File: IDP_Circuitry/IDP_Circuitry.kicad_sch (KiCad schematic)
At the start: 4 parts, among them U2 CD4093BE

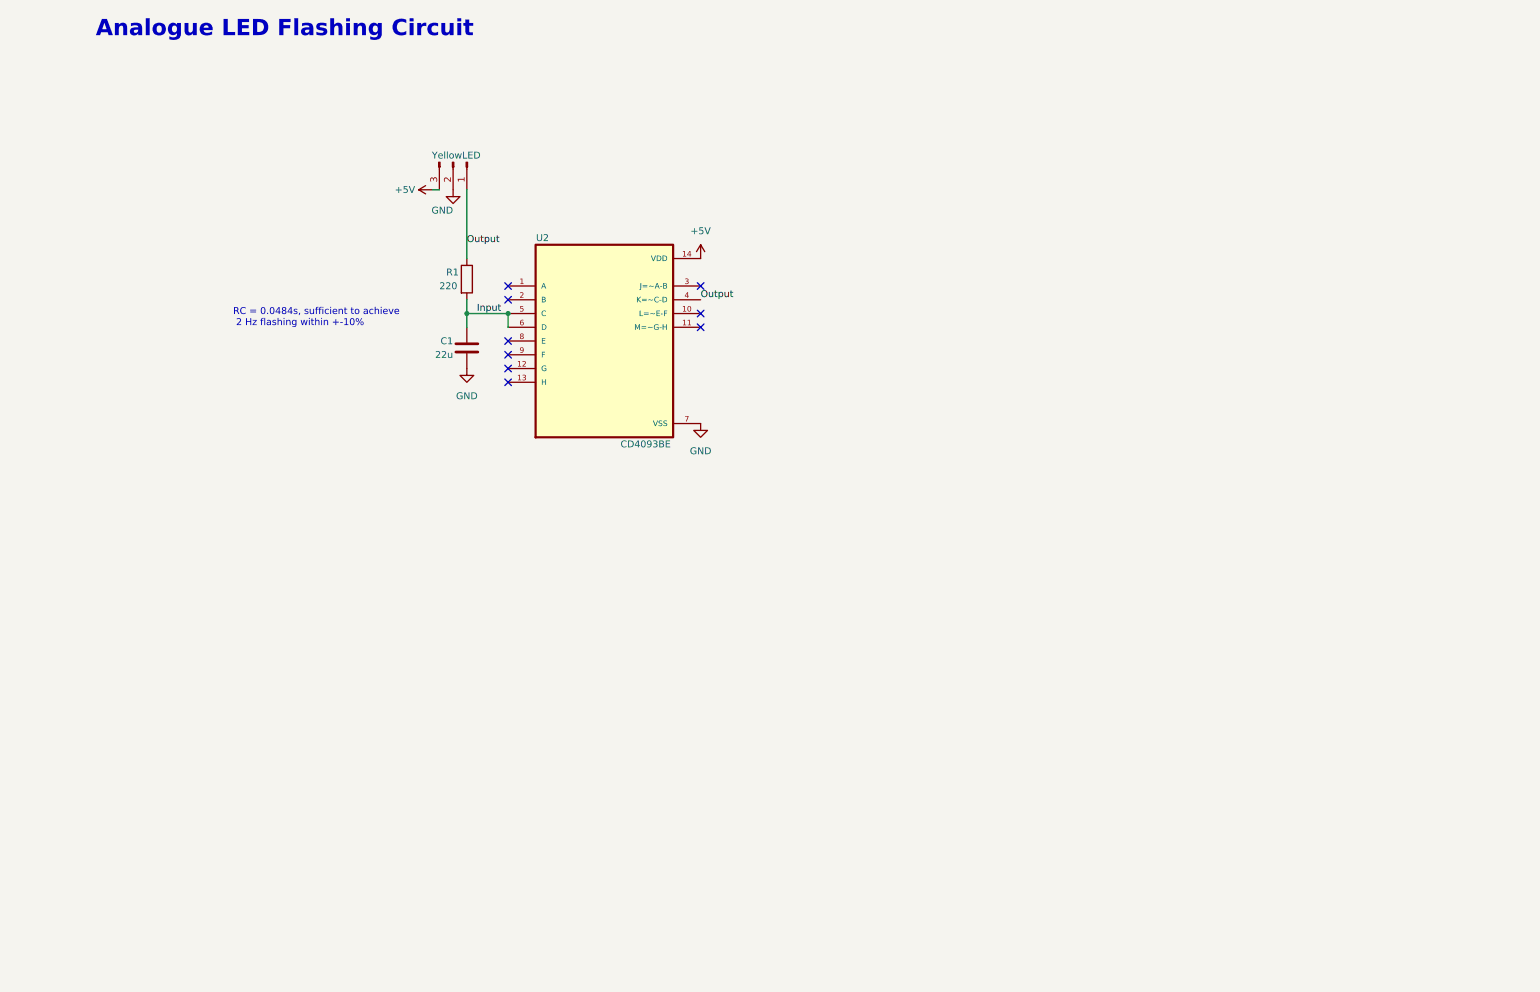
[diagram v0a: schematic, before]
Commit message: Corrected resistor values, changed schmitt NAND gate used, and adjusted schematic to fit all components on the same sheet
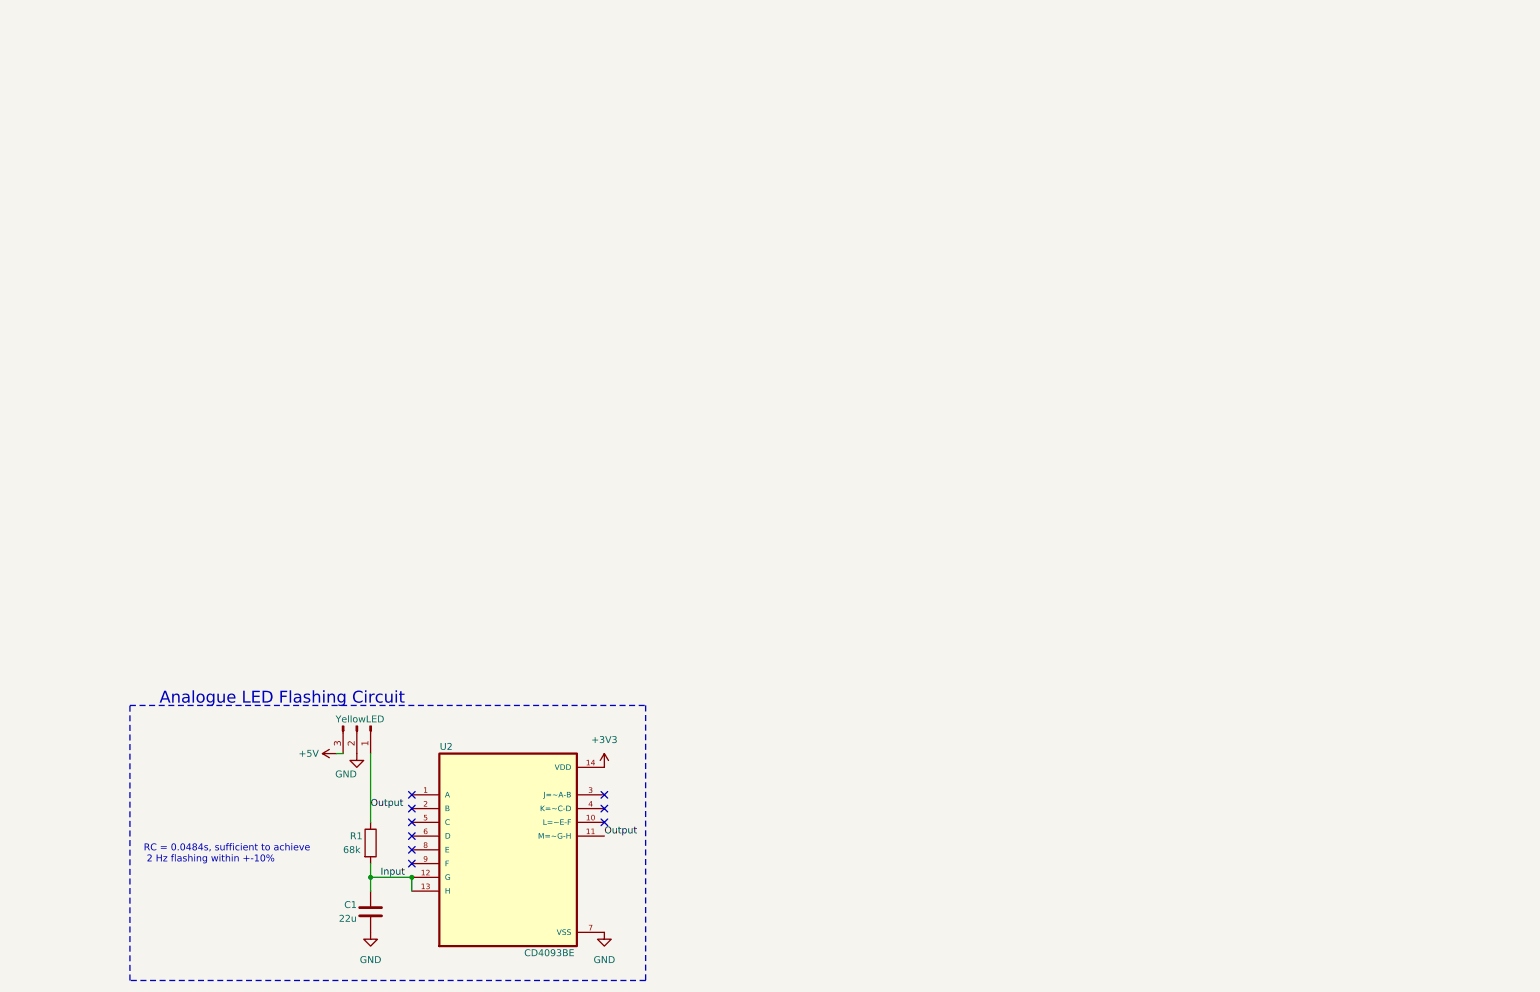
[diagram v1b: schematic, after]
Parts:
- R1: value 220 -> 68k
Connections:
- net +5V: no longer U2.14 (VDD)
- net Input: now also U2.12 (G), U2.13 (H); no longer U2.5 (C), U2.6 (D)
- net Output: now also U2.11 (M=~G-H); no longer U2.4 (K=~C-D)
- new net +3V3: U2.14 (VDD)
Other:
- title: LED Flashing Circuit -> Interface Board
- moved on the sheet: C1, R1, U2, YellowLED

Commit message: added schematics for the pinout board, line tracking sensors and added a button to the LED flasher
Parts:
- added A1: RaspberryPi_Pico_W, Module:RaspberryPi_Pico_W_SMD_HandSolder, symbol MCU_Module:RaspberryPi_Pico_W
- added J01, J02: Conn_01x20, symbol Connector_Generic:Conn_01x20
- added J1: PushButton, symbol Connector:Conn_01x03_Pin
- added J2: LineTrackerSensor1, symbol Connector:Conn_01x03_Pin
- added J3: LineTrackerSensor2, symbol Connector:Conn_01x03_Pin
- added J4: LineTrackerSensor3, symbol Connector:Conn_01x03_Pin
- added J5: LineTrackerSensor4, symbol Connector:Conn_01x03_Pin
- added J6: UltrasonicDistanceSensor, symbol Connector:Conn_01x03_Pin
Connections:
- net GND: now also A1.13 (GND), A1.18 (GND), A1.23 (GND), A1.28 (GND), A1.3 (GND), A1.38 (GND), A1.8 (GND), J01.13 (Pin_13), J01.18 (Pin_18), J01.3 (Pin_3), J01.8 (Pin_8), J02.23 (Pin_18), J02.28 (Pin_13), J02.33 (Pin_8), J02.38 (Pin_3), J1.3 (Pin_3), J2.3 (Pin_3), J3.3 (Pin_3), J4.3 (Pin_3), J5.3 (Pin_3)
- net Input: now also J1.1 (Pin_1)
- net +3V3: no longer names the net of U2.14 (VDD)
- new net 3V3(OUT): A1.36 (3V3), J02.36 (Pin_5), J1.2 (Pin_2), J2.2 (Pin_2), J3.2 (Pin_2), J4.2 (Pin_2), J5.2 (Pin_2)
- new net 3V3_EN: A1.37 (3V3_EN), J02.37 (Pin_4)
- new net ADC_VREF: A1.35 (ADC_VREF), J02.35 (Pin_6)
- new net GPIO0: A1.1 (GPIO0), J01.1 (Pin_1)
- new net GPIO1: A1.2 (GPIO1), J01.2 (Pin_2)
- new net GPIO10: A1.14 (GPIO10), J01.14 (Pin_14)
- new net GPIO11: A1.15 (GPIO11), J01.15 (Pin_15)
- new net GPIO12: A1.16 (GPIO12), J01.16 (Pin_16)
- new net GPIO13: A1.17 (GPIO13), J01.17 (Pin_17)
- new net GPIO14: A1.19 (GPIO14), J01.19 (Pin_19)
- new net GPIO15: A1.20 (GPIO15), J01.20 (Pin_20)
- new net GPIO16: A1.21 (GPIO16), J02.21 (Pin_20)
- new net GPIO17: A1.22 (GPIO17), J02.22 (Pin_19)
- new net GPIO18: A1.24 (GPIO18), J02.24 (Pin_17), J2.1 (Pin_1)
- new net GPIO19: A1.25 (GPIO19), J02.25 (Pin_16), J3.1 (Pin_1)
- new net GPIO2: A1.4 (GPIO2), J01.4 (Pin_4)
- new net GPIO20: A1.26 (GPIO20), J02.26 (Pin_15), J4.1 (Pin_1)
- new net GPIO21: A1.27 (GPIO21), J02.27 (Pin_14), J5.1 (Pin_1)
- new net GPIO22: A1.29 (GPIO22), J02.29 (Pin_12)
- new net GPIO26: A1.31 (GPIO26_ADC0), J02.31 (Pin_10)
- new net GPIO27: A1.32 (GPIO27_ADC1), J02.32 (Pin_9)
- new net GPIO28: A1.34 (GPIO28_ADC2), J02.34 (Pin_7)
- new net GPIO3: A1.5 (GPIO3), J01.5 (Pin_5)
- new net GPIO4: A1.6 (GPIO4), J01.6 (Pin_6)
- new net GPIO5: A1.7 (GPIO5), J01.7 (Pin_7)
- new net GPIO6: A1.9 (GPIO6), J01.9 (Pin_9)
- new net GPIO7: A1.10 (GPIO7), J01.10 (Pin_10)
- new net GPIO8: A1.11 (GPIO8), J01.11 (Pin_11)
- new net GPIO9: A1.12 (GPIO9), J01.12 (Pin_12)
- new net RUN: A1.30 (RUN), J02.30 (Pin_11)
- new net VBUS: A1.40 (VBUS), J02.40 (Pin_1)
- new net VSYS: A1.39 (VSYS), J02.39 (Pin_2)
- no-connect marks 9 -> 19
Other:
- note added: "LTC"
- note added: "Line Tracker Circuit (LTC)"
- note added: "Pico W"
- note added: "Pico W Breakout Pins"

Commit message: added all footprints, added libraryIDP for flipped pin header schematic
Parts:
- C1: footprint (none) -> Capacitor_THT:C_Radial_D5.0mm_H5.0mm_P2.00mm
- LineTracker1: renamed from J2; value LineTrackerSensor1 -> Conn_01x03_Pin; footprint (none) -> Connector_PinSocket_2.54mm:PinSocket_1x03_P2.54mm_Vertical
- LineTracker2: renamed from J3; value LineTrackerSensor2 -> Conn_01x03_Pin; footprint (none) -> Connector_PinSocket_2.54mm:PinSocket_1x03_P2.54mm_Vertical
- LineTracker3: renamed from J4; value LineTrackerSensor3 -> Conn_01x03_Pin; footprint (none) -> Connector_PinSocket_2.54mm:PinSocket_1x03_P2.54mm_Vertical
- LineTracker4: renamed from J5; value LineTrackerSensor4 -> Conn_01x03_Pin; footprint (none) -> Connector_PinSocket_2.54mm:PinSocket_1x03_P2.54mm_Vertical
- Pico_W1: renamed from A1; footprint Module:RaspberryPi_Pico_W_SMD_HandSolder -> Module:RaspberryPi_Pico_Common_THT
- PinoutL1: renamed from J01; footprint (none) -> Connector_PinHeader_2.54mm:PinHeader_1x20_P2.54mm_Vertical
- PinoutR1: renamed from J02; footprint (none) -> LibraryIDP:PinHeader_1x20_P2.54mm_Vertical_Flipped_21-40
- PushButton1: renamed from J1; value PushButton -> Conn_01x03_Pin; footprint (none) -> Connector_PinSocket_2.54mm:PinSocket_1x03_P2.54mm_Vertical
- R1: footprint (none) -> Resistor_THT:R_Axial_DIN0207_L6.3mm_D2.5mm_P2.54mm_Vertical
- UltrasonicDistanceSensor1: renamed from J6; value UltrasonicDistanceSensor -> Conn_01x03_Pin; footprint (none) -> Connector_PinSocket_2.54mm:PinSocket_1x03_P2.54mm_Vertical
- YellowLED1: renamed from YellowLED; footprint (none) -> Connector_PinSocket_2.54mm:PinSocket_1x03_P2.54mm_Vertical
- renumbered U2 to SchmittTrigger1
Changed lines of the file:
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@@
 		(polyline
 			(pts
-				(xy 200.66 49.53) (xy 200.66 59.69) (xy 184.15 59.69) (xy 184.15 49.53)
+				(xy 25.4 25.4) (xy 25.4 82.55) (xy 54.61 82.55) (xy 54.61 25.4)
+			)
+			(stroke
+				(width 0.254)
+				(type dash)
+				(color 0 0 194 1)
+			)
+			(fill
+				(type none)
+			)
+		)
+	)
+	(rule_area
+		(polyline
+			(pts
+				(xy 144.78 54.61) (xy 144.78 67.31) (xy 161.29 67.31) (xy 161.29 54.61)
 			)
 			(stroke
@@
 		(polyline
 			(pts
-				(xy 25.4 25.4) (xy 25.4 82.55) (xy 54.61 82.55) (xy 54.61 25.4)
+				(xy 200.66 49.53) (xy 200.66 59.69) (xy 184.15 59.69) (xy 184.15 49.53)
 			)
 			(stroke
-				(width 0.254)
+				(width 0.1778)
+				(type dash)
+				(color 0 0 194 1)
+			)
+			(fill
+				(type none)
+			)
+		)
+	)
+	(rule_area
+		(polyline
+			(pts
+				(xy 276.86 20.32) (xy 210.82 20.32) (xy 210.82 107.95) (xy 276.86 107.95)
+			)
+			(stroke
+				(width 0.1778)
 				(type dash)
 				(color 0 0 194 1)
@@
 		)
 	)
-	(rule_area
-		(polyline
-			(pts
-				(xy 276.86 20.32) (xy 210.82 20.32) (xy 210.82 107.95) (xy 276.86 107.95)
-			)
-			(stroke
-				(width 0.1778)
-				(type dash)
-				(color 0 0 194 1)
-			)
-			(fill
-				(type none)
-			)
-		)
-	)
-	(rule_area
-		(polyline
-			(pts
-				(xy 144.78 54.61) (xy 144.78 67.31) (xy 161.29 67.31) (xy 161.29 54.61)
-			)
-			(stroke
-				(width 0.1778)
-				(type dash)
-				(color 0 0 194 1)
-			)
-			(fill
-				(type none)
-			)
-		)
-	)
 	(symbol
 		(lib_name "GND_2")
@@
 		(dnp no)
 		(fields_autoplaced yes)
-		(property "Reference" "J6"
+		(property "Reference" "UltrasonicDistanceSensor1"
 			(at 147.955 175.26 0)
 			(effects
@@
 			)
 		)
-		(property "Value" "UltrasonicDistanceSensor"
+		(property "Value" "Conn_01x03_Pin"
 			(at 147.955 177.8 0)
 			(effects
@@
 			)
 		)
-		(property "Footprint" ""
+		(property "Footprint" "Connector_PinSocket_2.54mm:PinSocket_1x03_P2.54mm_Vertical"
 			(at 147.32 182.88 0)
 			(effects
@@
 			(project "IDP_Circuitry"
 				(path "/5a0366d0-ccf7-45ad-b08f-1738d84a7d2e"
-					(reference "J6")
+					(reference "UltrasonicDistanceSensor1")
 					(unit 1)
 				)
@@
 		(on_board yes)
 		(dnp no)
-		(property "Reference" "J02"
+		(property "Reference" "PinoutR1"
 			(at 184.15 28.702 0)
 			(effects
@@
 			)
 		)
-		(property "Footprint" ""
+		(property "Footprint" "LibraryIDP:PinHeader_1x20_P2.54mm_Vertical_Flipped_21-40"
 			(at 184.15 54.61 0)
 			(effects
@@
 			(project ""
 				(path "/5a0366d0-ccf7-45ad-b08f-1738d84a7d2e"
-					(reference "J02")
+					(reference "PinoutR1")
 					(unit 1)
 				)
@@
 		(on_board yes)
 		(dnp no)
-		(property "Reference" "YellowLED"
+		(property "Reference" "YellowLED1"
 			(at 66.04 143.51 90)
 			(effects
@@
 			)
 		)
-		(property "Footprint" ""
+		(property "Footprint" "Connector_PinSocket_2.54mm:PinSocket_1x03_P2.54mm_Vertical"
 			(at 60.96 144.78 0)
 			(effects
@@
 			(project "IDP_Circuitry"
 				(path "/5a0366d0-ccf7-45ad-b08f-1738d84a7d2e"
-					(reference "YellowLED")
+					(reference "YellowLED1")
 					(unit 1)
 				)
@@
 		(dnp no)
 		(fields_autoplaced yes)
-		(property "Reference" "J1"
+		(property "Reference" "PushButton1"
 			(at 29.845 143.51 0)
 			(effects
@@
 			)
 		)
-		(property "Value" "PushButton"
+		(property "Value" "Conn_01x03_Pin"
 			(at 29.845 146.05 0)
 			(effects
@@
 			)
 		)
-		(property "Footprint" ""
+		(property "Footprint" "Connector_PinSocket_2.54mm:PinSocket_1x03_P2.54mm_Vertical"
 			(at 29.21 151.13 0)
 			(effects
@@
 			(project ""
 				(path "/5a0366d0-ccf7-45ad-b08f-1738d84a7d2e"
-					(reference "J1")
+					(reference "PushButton1")
 					(unit 1)
 				)
@@
 		(dnp no)
 		(fields_autoplaced yes)
-		(property "Reference" "J2"
+		(property "Reference" "LineTracker1"
 			(at 37.465 29.21 0)
 			(effects
@@
 			)
 		)
-		(property "Value" "LineTrackerSensor1"
+		(property "Value" "Conn_01x03_Pin"
 			(at 37.465 31.75 0)
 			(effects
@@
 			)
 		)
-		(property "Footprint" ""
+		(property "Footprint" "Connector_PinSocket_2.54mm:PinSocket_1x03_P2.54mm_Vertical"
 			(at 36.83 36.83 0)
 			(effects
@@
 			(project "IDP_Circuitry"
 				(path "/5a0366d0-ccf7-45ad-b08f-1738d84a7d2e"
-					(reference "J2")
+					(reference "LineTracker1")
 					(unit 1)
 				)
@@
 		(on_board yes)
 		(dnp no)
-		(property "Reference" "U2"
+		(property "Reference" "SchmittTrigger1"
 			(at 77.47 148.59 0)
 			(effects
@@
 			)
 		)
-		(property "Description" "\n                        \n                            4-ch, 2-input, 3-V to 18-V NAND gates with Schmitt-Trigger inputs\n                        \n"
+		(property "Description" "4-ch, 2-input, 3-V to 18-V NAND gates with Schmitt-Trigger inputs"
 			(at 88.9 167.64 0)
 			(effects
@@
 			(project "IDP_Circuitry"
 				(path "/5a0366d0-ccf7-45ad-b08f-1738d84a7d2e"
-					(reference "U2")
+					(reference "SchmittTrigger1")
 					(unit 1)
 				)
@@
 			)
 		)
-		(property "Footprint" ""
+		(property "Footprint" "Resistor_THT:R_Axial_DIN0207_L6.3mm_D2.5mm_P2.54mm_Vertical"
 			(at 61.722 166.37 90)
 			(effects
@@
 		(dnp no)
 		(fields_autoplaced yes)
-		(property "Reference" "J5"
+		(property "Reference" "LineTracker4"
 			(at 37.465 69.85 0)
 			(effects
@@
 			)
 		)
-		(property "Value" "LineTrackerSensor4"
+		(property "Value" "Conn_01x03_Pin"
 			(at 37.465 72.39 0)
 			(effects
@@
 			)
 		)
-		(property "Footprint" ""
+		(property "Footprint" "Connector_PinSocket_2.54mm:PinSocket_1x03_P2.54mm_Vertical"
 			(at 36.83 77.47 0)
 			(effects
@@
 			(project "IDP_Circuitry"
 				(path "/5a0366d0-ccf7-45ad-b08f-1738d84a7d2e"
-					(reference "J5")
+					(reference "LineTracker4")
 					(unit 1)
 				)
@@
 			)
 		)
-		(property "Footprint" ""
+		(property "Footprint" "Capacitor_THT:C_Radial_D5.0mm_H5.0mm_P2.00mm"
 			(at 64.4652 182.88 0)
 			(effects
@@
 		(dnp no)
 		(fields_autoplaced yes)
-		(property "Reference" "A1"
+		(property "Reference" "Pico_W1"
 			(at 245.9833 102.87 0)
 			(effects
@@
 			)
 		)
-		(property "Footprint" "Module:RaspberryPi_Pico_W_SMD_HandSolder"
+		(property "Footprint" "Module:RaspberryPi_Pico_Common_THT"
 			(at 243.84 115.57 0)
 			(effects
@@
 			(project ""
 				(path "/5a0366d0-ccf7-45ad-b08f-1738d84a7d2e"
-					(reference "A1")
+					(reference "Pico_W1")
 					(unit 1)
 				)
@@
 		(dnp no)
 		(fields_autoplaced yes)
-		(property "Reference" "J3"
+		(property "Reference" "LineTracker2"
 			(at 37.465 41.91 0)
 			(effects
@@
 			)
 		)
-		(property "Value" "LineTrackerSensor2"
+		(property "Value" "Conn_01x03_Pin"
 			(at 37.465 44.45 0)
 			(effects
@@
 			)
 		)
-		(property "Footprint" ""
+		(property "Footprint" "Connector_PinSocket_2.54mm:PinSocket_1x03_P2.54mm_Vertical"
 			(at 36.83 49.53 0)
 			(effects
@@
 			(project "IDP_Circuitry"
 				(path "/5a0366d0-ccf7-45ad-b08f-1738d84a7d2e"
-					(reference "J3")
+					(reference "LineTracker2")
 					(unit 1)
 				)
@@
 		(dnp no)
 		(fields_autoplaced yes)
-		(property "Reference" "J4"
+		(property "Reference" "LineTracker3"
 			(at 37.465 55.88 0)
 			(effects
@@
 			)
 		)
-		(property "Value" "LineTrackerSensor3"
+		(property "Value" "Conn_01x03_Pin"
 			(at 37.465 58.42 0)
 			(effects
@@
 			)
 		)
-		(property "Footprint" ""
+		(property "Footprint" "Connector_PinSocket_2.54mm:PinSocket_1x03_P2.54mm_Vertical"
 			(at 36.83 63.5 0)
 			(effects
@@
 			(project "IDP_Circuitry"
 				(path "/5a0366d0-ccf7-45ad-b08f-1738d84a7d2e"
-					(reference "J4")
+					(reference "LineTracker3")
 					(unit 1)
 				)
@@
 		(on_board yes)
 		(dnp no)
-		(property "Reference" "J01"
+		(property "Reference" "PinoutL1"
 			(at 161.036 28.702 0)
 			(effects
@@
 			)
 		)
-		(property "Footprint" ""
+		(property "Footprint" "Connector_PinHeader_2.54mm:PinHeader_1x20_P2.54mm_Vertical"
 			(at 161.29 54.61 0)
 			(effects
@@
 			(project ""
 				(path "/5a0366d0-ccf7-45ad-b08f-1738d84a7d2e"
-					(reference "J01")
-					(unit 1)
-				)
+					(reference "PinoutL1")
+					(unit 1)
+				)

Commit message: updated pcb, need to change footprint to make the ic compatible with the pinout board holes
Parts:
- removed UltrasonicDistanceSensor1: Conn_01x03_Pin, Connector_PinSocket_2.54mm:PinSocket_1x03_P2.54mm_Vertical, symbol Connector:Conn_01x03_Pin
- added R2, R3: 4.7k, Resistor_THT:R_Axial_DIN0204_L3.6mm_D1.6mm_P2.54mm_Vertical, symbol Device:R
- added ToFSensor1: Conn_01x04_Pin, Connector_PinSocket_2.54mm:PinSocket_1x04_P2.54mm_Vertical, symbol Connector:Conn_01x04_Pin
- C1: footprint Capacitor_THT:C_Radial_D5.0mm_H5.0mm_P2.00mm -> Capacitor_THT:C_Radial_D4.0mm_H5.0mm_P1.50mm
- R1: footprint Resistor_THT:R_Axial_DIN0207_L6.3mm_D2.5mm_P2.54mm_Vertical -> Resistor_THT:R_Axial_DIN0204_L3.6mm_D1.6mm_P2.54mm_Vertical
- SchmittTrigger1: footprint CD4093BE:DIP794W45P254L1969H508Q14 -> CD4093BE:CD4093BE
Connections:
- net +5V is gone; now on net GND: YellowLED1.3 (Pin_3)
- net 3V3(OUT): now also YellowLED1.2 (Pin_2), R2.2, R3.2, ToFSensor1.4 (Pin_4)
- net GND: now also ToFSensor1.3 (Pin_3); no longer YellowLED1.2 (Pin_2)
- net GPIO8: now also R2.1, ToFSensor1.1 (Pin_1)
- net GPIO9: now also R3.1, ToFSensor1.2 (Pin_2)
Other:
- note added: "I2C"

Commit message: completed updates schematic and wired all components on the pcb. Minor tweaks likely necessary, but overall complete
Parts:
- added ColourSensor1: Conn_01x04_Pin, Connector_PinSocket_2.54mm:PinSocket_1x04_P2.54mm_Vertical, symbol Connector:Conn_01x04_Pin
- added R4, R5: 4.7k, Resistor_THT:R_Axial_DIN0204_L3.6mm_D1.6mm_P2.54mm_Vertical, symbol Device:R
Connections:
- net 3V3(OUT): now also SchmittTrigger1.14 (VDD), ColourSensor1.4 (Pin_4), R4.2, R5.2
- net GND: now also ColourSensor1.3 (Pin_3)
- net GPIO10: now also ColourSensor1.1 (Pin_1), R4.1
- net GPIO11: now also ColourSensor1.2 (Pin_2), R5.1
- net GPIO14: now also SchmittTrigger1.13 (H)
- net GPIO22: now also PushButton1.1 (Pin_1)
- net Input: no longer PushButton1.1 (Pin_1), SchmittTrigger1.13 (H)
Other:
- note added: "IO"
- moved on the sheet: PushButton1

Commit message: final commit, completed schematic/pcb and fully labelled
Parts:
- SchmittTrigger1: footprint CD4093BE:CD4093BE -> CD4093BE:DIP794W45P254L1969H508Q14
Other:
- moved on the sheet: C1, ColourSensor1, LineTracker1, LineTracker2, LineTracker3, LineTracker4, Pico_W1, PinoutL1, PinoutR1, PushButton1, R1, R2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
